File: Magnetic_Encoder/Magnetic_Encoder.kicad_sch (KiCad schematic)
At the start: 2 parts, among them J1 Conn_01x04, U1 TLV493D-A1B6

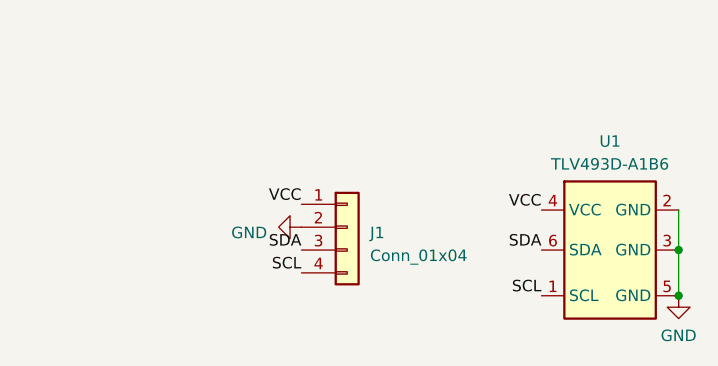
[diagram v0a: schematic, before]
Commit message: Finalized compact magnetic encoder design
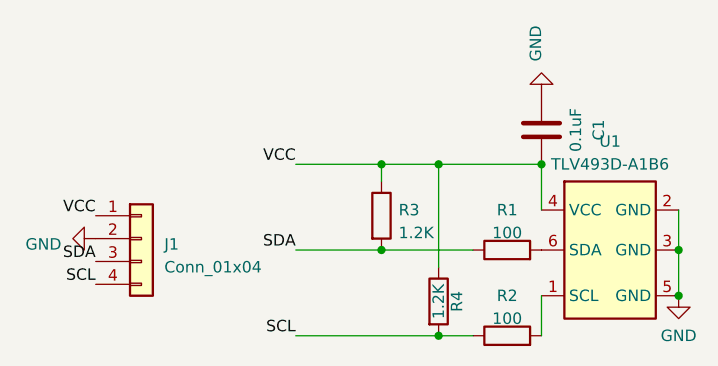
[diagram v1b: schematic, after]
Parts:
- added C1: 0.1uF, Capacitor_SMD:C_0402_1005Metric, symbol Device:C
- added R1, R2: 100, Resistor_SMD:R_0402_1005Metric, symbol Device:R
- added R3, R4: 1.2K, Resistor_SMD:R_0402_1005Metric, symbol Device:R
- J1: footprint Connector_PinHeader_2.54mm:PinHeader_1x04_P2.54mm_Horizontal -> Connector_PinSocket_2.54mm:PinSocket_1x04_P2.54mm_Horizontal
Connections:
- net GND: now also C1.1
- net SCL: now also R2.1, R4.2; no longer U1.1 (SCL)
- net SDA: now also R1.1, R3.2; no longer U1.6 (SDA)
- net VCC: now also C1.2, R3.1, R4.1
- new net: R2.2, U1.1 (SCL)
- new net: R1.2, U1.6 (SDA)
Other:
- moved on the sheet: J1
